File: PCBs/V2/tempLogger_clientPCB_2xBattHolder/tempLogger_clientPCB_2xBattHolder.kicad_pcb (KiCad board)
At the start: 2 copper layers, 72.4 x 102.9 mm, 6 parts

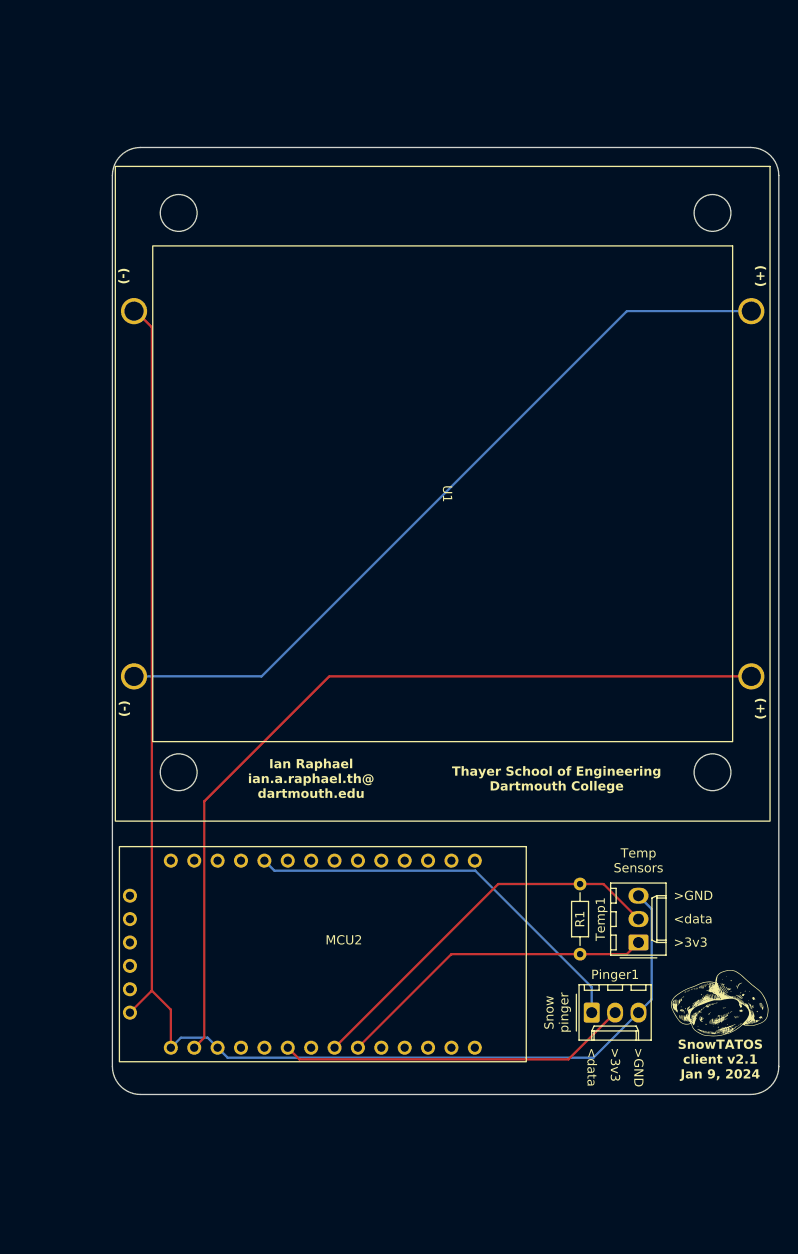
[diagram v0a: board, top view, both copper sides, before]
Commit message: fixed pinger read error
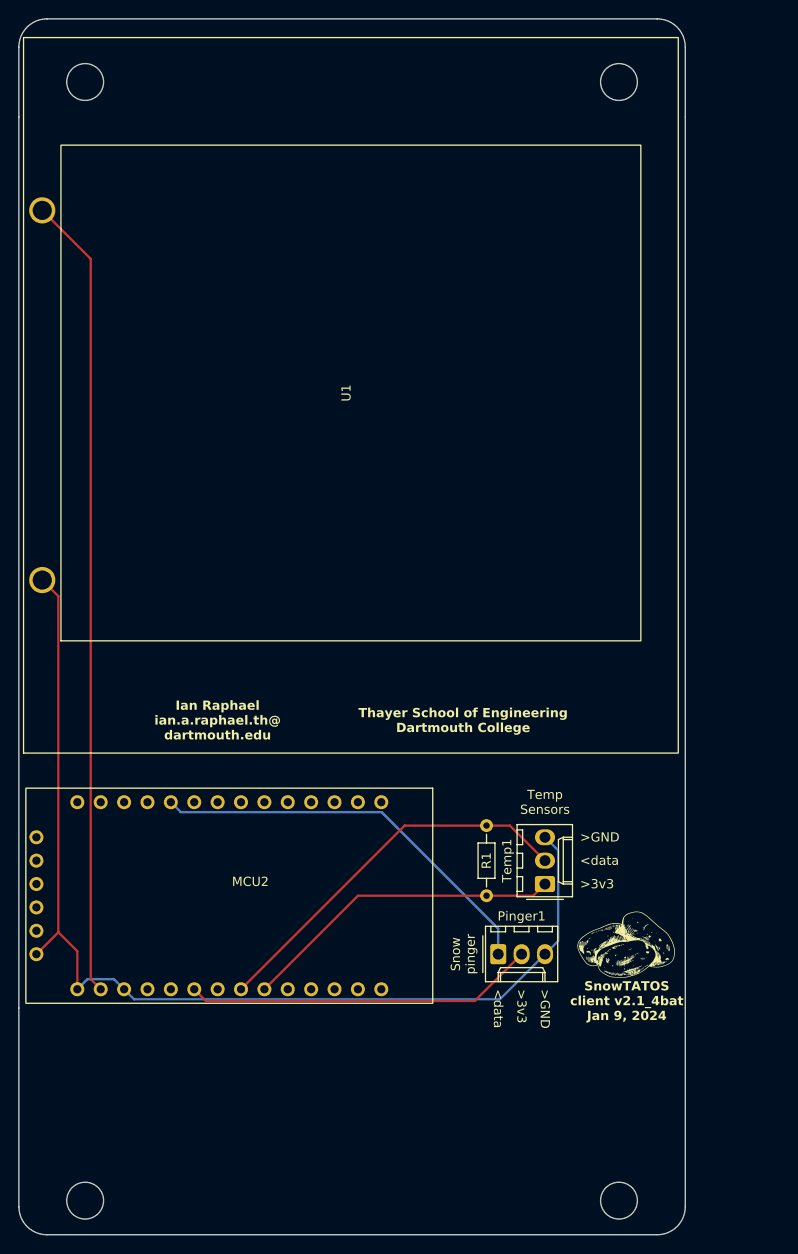
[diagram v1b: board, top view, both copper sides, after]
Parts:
- U1: value ~ -> keystone_2233_D_cell_4Batt_holder; footprint Battery:BatteryHolder_Keystone_2233 -> Battery:BatteryHolder_Keystone_2233_4Cell
- moved U1 14.8 mm to (132.6, 71.1), turned to 90 degrees
- moved Temp1 12.0 mm to (153.7, 124.5)
- moved MCU2 12.0 mm to (115.6, 125.7)
- moved R1 12.0 mm to (147.3, 125.7)
- moved G*** 12.0 mm to (162.6, 130.8)
- moved Pinger1 12.0 mm to (148.6, 132.1)
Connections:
- U1 pad 0: Net-(U1-Pad0) -> /GND
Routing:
- net Net-(U1-Pad0): track 83.1 -> 0.00 mm
- net /GND: track 153.0 -> 117.5 mm
- net /VBAT: track 92.1 -> 87.2 mm
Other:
- board size 72.4 x 102.9 mm -> 72.4 x 132.1 mm
- board text added: "SnowTATOS client v2.1_4bat Jan 9, 2024"
- board text removed: "(+)"
- board text removed: "(-)"
- board text removed: "SnowTATOS client v2.1 Jan 9, 2024"
